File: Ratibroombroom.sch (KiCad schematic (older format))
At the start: 116 parts, among them J1 Conn_01x02_Male, J10 Conn_01x04_Male, J11 Conn_01x04_Male, J12 Support board base, J13 Support board base, J2 Conn_01x02_Male, J3 Conn_01x10_Male, J4 Support board axle, J5 Conn_01x02_Male, J6 Conn_01x02_Male, J7 Support board axle, J8 Conn_01x04_Male, J9 Conn_01x04_Male, Q1 IRLML6344, Q10 S8050, Q11 IRF7416PbF, Q2 IRLML6344, Q3 IRLML6344, Q4 IRLML6344, Q5 PT12-21B/TR8, Q6 PT12-21B/TR8, Q7 PT12-21B/TR8, Q8 PT12-21B/TR8, Q9 IRLML6344, SW1 B3U, SW2 B3U, SW3 PCM12, U1 AZ1117-3.3, U2 DRV8835, U3 AS5145B-HSST, U4 MPU-9250, U5 STM32F405RGTx, U6 AS5145B-HSST, U7 DRV8835, U8 L6932D1.2TR, U9 L6932D1.2TR, Y1 8MHZ

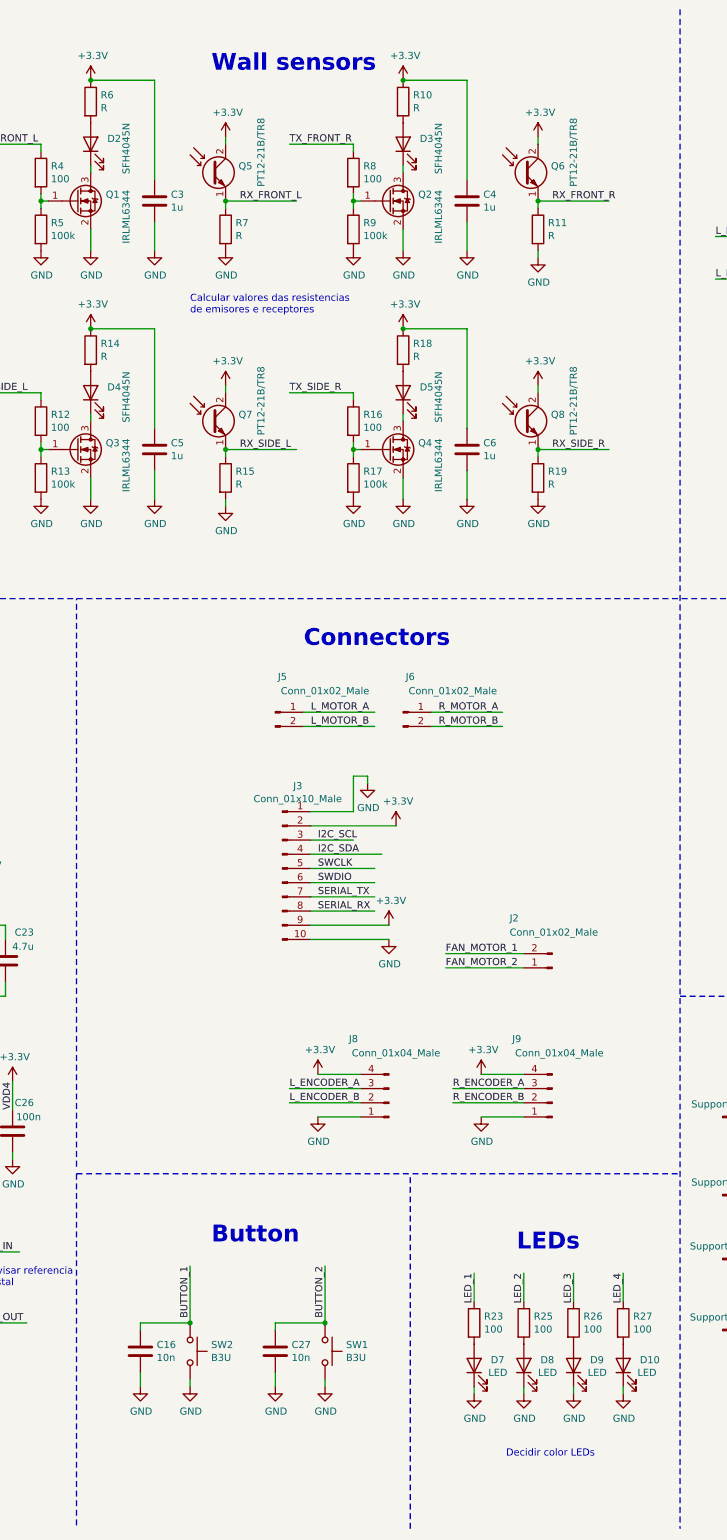
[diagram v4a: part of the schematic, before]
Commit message: Add BOM references
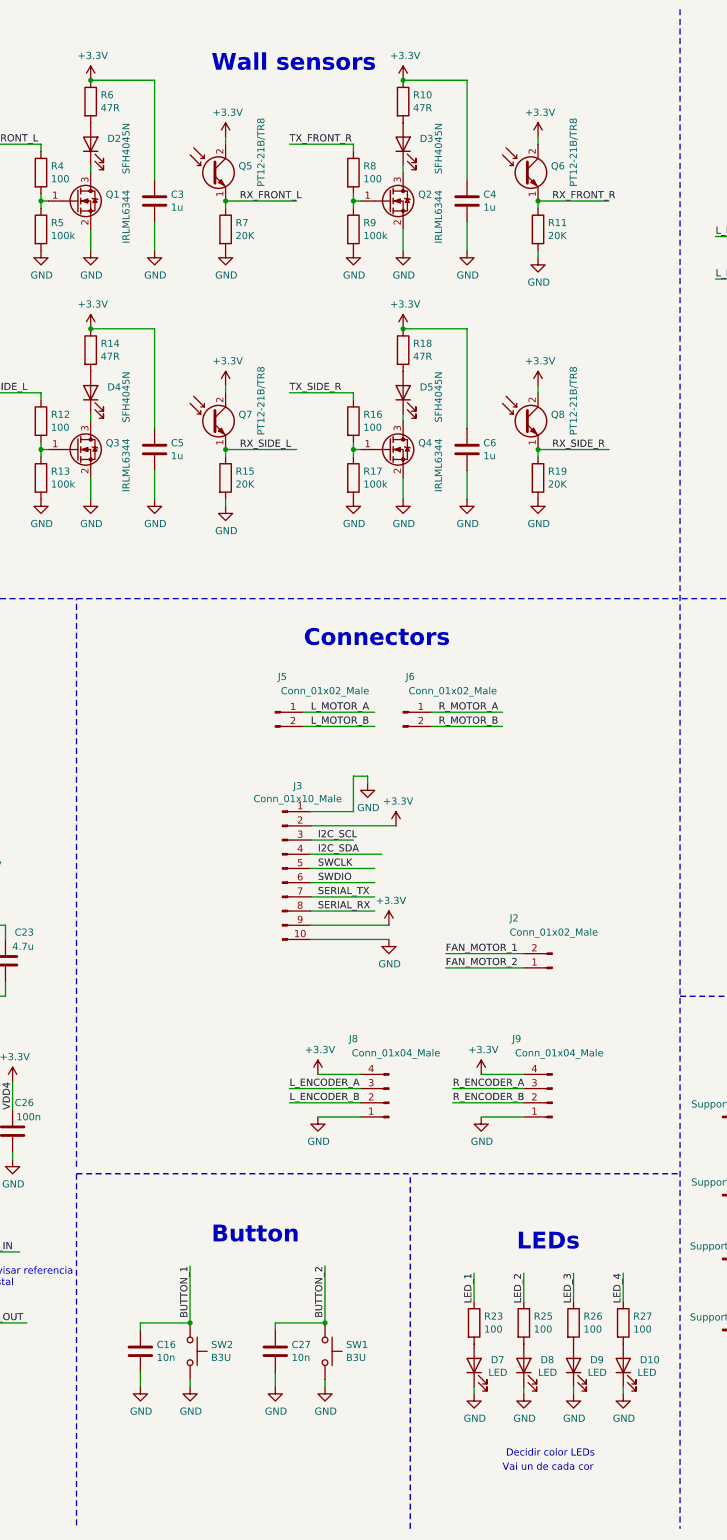
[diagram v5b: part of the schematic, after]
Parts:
- D10: MFR (none) -> 19-217/BHC-ZL1M2RY/3T; Note (none) -> Blue
- D7: MFR (none) -> LTW-C193DS5; Note (none) -> White
- D8: MFR (none) -> 19-217/R6C-AL1M2VY/3T; Note (none) -> Red
- D9: MFR (none) -> ORH-G36G; Note (none) -> Green
- J3: MFR (none) -> 20021111-00010T4LF; Note (none) -> Female: 2343U-205CNG1SNT01
- R10, R14, R18, R6: value R -> 47R; MFR (none) -> CR0603FA47R0G
- R11, R15, R19, R7: value R -> 20K; MFR (none) -> RK73H1JTTD2002F
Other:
- note added: "Vai un de cada cor"
- note removed: "Calcular valores das resistencias\nde emisores e receptores"
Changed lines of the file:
@@
 P 7150 2050
 F 0 "R7" H 7220 2096 50  0000 L CNN
-F 1 "R" H 7220 2005 50  0000 L CNN
+F 1 "20K" H 7220 2005 50  0000 L CNN
 F 2 "Resistor_SMD:R_0603_1608Metric" V 7080 2050 50  0001 C CNN
 F 3 "~" H 7150 2050 50  0001 C CNN
+F 4 "RK73H1JTTD2002F" H 7150 2050 50  0001 C CNN "MFR"
 	1    7150 2050
 	1    0    0    -1
@@
 P 6200 1150
 F 0 "R6" H 6270 1196 50  0000 L CNN
-F 1 "R" H 6270 1105 50  0000 L CNN
+F 1 "47R" H 6270 1105 50  0000 L CNN
 F 2 "Resistor_SMD:R_0603_1608Metric" V 6130 1150 50  0001 C CNN
 F 3 "~" H 6200 1150 50  0001 C CNN
+F 4 "CR0603FA47R0G" H 6200 1150 50  0001 C CNN "MFR"
 	1    6200 1150
 	1    0    0    -1
@@
 P 9350 2050
 F 0 "R11" H 9420 2096 50  0000 L CNN
-F 1 "R" H 9420 2005 50  0000 L CNN
+F 1 "20K" H 9420 2005 50  0000 L CNN
 F 2 "Resistor_SMD:R_0603_1608Metric" V 9280 2050 50  0001 C CNN
 F 3 "~" H 9350 2050 50  0001 C CNN
+F 4 "RK73H1JTTD2002F" H 9350 2050 50  0001 C CNN "MFR"
 	1    9350 2050
 	1    0    0    -1
@@
 P 8400 1150
 F 0 "R10" H 8470 1196 50  0000 L CNN
-F 1 "R" H 8470 1105 50  0000 L CNN
+F 1 "47R" H 8470 1105 50  0000 L CNN
 F 2 "Resistor_SMD:R_0603_1608Metric" V 8330 1150 50  0001 C CNN
 F 3 "~" H 8400 1150 50  0001 C CNN
+F 4 "CR0603FA47R0G" H 8400 1150 50  0001 C CNN "MFR"
 	1    8400 1150
 	1    0    0    -1
@@
 P 7150 3800
 F 0 "R15" H 7220 3846 50  0000 L CNN
-F 1 "R" H 7220 3755 50  0000 L CNN
+F 1 "20K" H 7220 3755 50  0000 L CNN
 F 2 "Resistor_SMD:R_0603_1608Metric" V 7080 3800 50  0001 C CNN
 F 3 "~" H 7150 3800 50  0001 C CNN
+F 4 "RK73H1JTTD2002F" H 7150 3800 50  0001 C CNN "MFR"
 	1    7150 3800
 	1    0    0    -1
@@
 P 6200 2900
 F 0 "R14" H 6270 2946 50  0000 L CNN
-F 1 "R" H 6270 2855 50  0000 L CNN
+F 1 "47R" H 6270 2855 50  0000 L CNN
 F 2 "Resistor_SMD:R_0603_1608Metric" V 6130 2900 50  0001 C CNN
 F 3 "~" H 6200 2900 50  0001 C CNN
+F 4 "CR0603FA47R0G" H 6200 2900 50  0001 C CNN "MFR"
 	1    6200 2900
 	1    0    0    -1
@@
 P 9350 3800
 F 0 "R19" H 9420 3846 50  0000 L CNN
-F 1 "R" H 9420 3755 50  0000 L CNN
+F 1 "20K" H 9420 3755 50  0000 L CNN
 F 2 "Resistor_SMD:R_0603_1608Metric" V 9280 3800 50  0001 C CNN
 F 3 "~" H 9350 3800 50  0001 C CNN
+F 4 "RK73H1JTTD2002F" H 9350 3800 50  0001 C CNN "MFR"
 	1    9350 3800
 	1    0    0    -1
@@
 P 8400 2900
 F 0 "R18" H 8470 2946 50  0000 L CNN
-F 1 "R" H 8470 2855 50  0000 L CNN
+F 1 "47R" H 8470 2855 50  0000 L CNN
 F 2 "Resistor_SMD:R_0603_1608Metric" V 8330 2900 50  0001 C CNN
 F 3 "~" H 8400 2900 50  0001 C CNN
+F 4 "CR0603FA47R0G" H 8400 2900 50  0001 C CNN "MFR"
 	1    8400 2900
 	1    0    0    -1
@@
 F 2 "LED_SMD:LED_0603_1608Metric" H 8900 10050 50  0001 C CNN
 F 3 "~" H 8900 10050 50  0001 C CNN
+F 4 "LTW-C193DS5" V 8900 10050 50  0001 C CNN "MFR"
+F 5 "White" V 8900 10050 50  0001 C CNN "Note"
 	1    8900 10050
 	0    -1   -1   0
@@
 F 2 "LED_SMD:LED_0603_1608Metric" H 9250 10050 50  0001 C CNN
 F 3 "~" H 9250 10050 50  0001 C CNN
+F 4 "19-217/R6C-AL1M2VY/3T" V 9250 10050 50  0001 C CNN "MFR"
+F 5 "Red" V 9250 10050 50  0001 C CNN "Note"
 	1    9250 10050
 	0    -1   -1   0
@@
 F 2 "LED_SMD:LED_0603_1608Metric" H 9600 10050 50  0001 C CNN
 F 3 "~" H 9600 10050 50  0001 C CNN
+F 4 "ORH-G36G" V 9600 10050 50  0001 C CNN "MFR"
+F 5 "Green" V 9600 10050 50  0001 C CNN "Note"
 	1    9600 10050
 	0    -1   -1   0
@@
 F 2 "LED_SMD:LED_0603_1608Metric" H 9950 10050 50  0001 C CNN
 F 3 "~" H 9950 10050 50  0001 C CNN
+F 4 "19-217/BHC-ZL1M2RY/3T" V 9950 10050 50  0001 C CNN "MFR"
+F 5 "Blue" V 9950 10050 50  0001 C CNN "Note"
 	1    9950 10050
 	0    -1   -1   0
@@
 	1    0    0    -1
 $EndComp
-Text Notes 6900 2650 0    50   ~ 0
-Calcular valores das resistencias\nde emisores e receptores
 $Comp
 L Connector:Conn_01x10_Male J3
@@
 F 2 "Connector_PinHeader_1.27mm:PinHeader_2x05_P1.27mm_Vertical" H 7550 6550 50  0001 C CNN
 F 3 "~" H 7550 6550 50  0001 C CNN
+F 4 "20021111-00010T4LF" H 7550 6550 50  0001 C CNN "MFR"
+F 5 "Female: 2343U-205CNG1SNT01" H 7550 6550 50  0001 C CNN "Note"
 	1    7550 6550
 	1    0    0    -1
@@
 Wire Wire Line
 	10950 9300 10850 9300
+Text Notes 9100 10800 0    50   ~ 0
+Vai un de cada cor
 $EndSCHEMATC

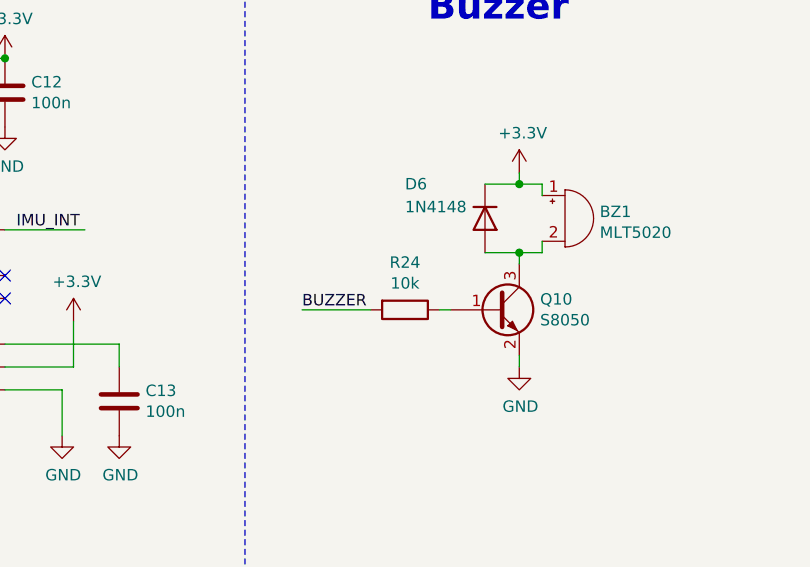
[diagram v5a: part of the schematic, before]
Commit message: Change R24 value to 1k8 to increase buzzer loudness
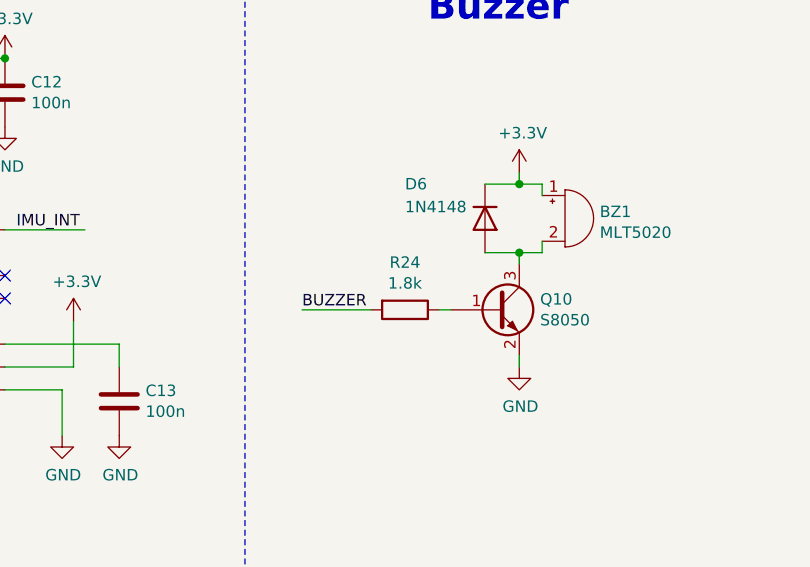
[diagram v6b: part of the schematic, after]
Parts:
- R24: value 10k -> 1.8k; MFR CR0603FA1002G -> 0603WAD1801T5E
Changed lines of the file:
@@
 P 14300 6250
 F 0 "R24" V 14093 6250 50  0000 C CNN
-F 1 "10k" V 14184 6250 50  0000 C CNN
+F 1 "1.8k" V 14184 6250 50  0000 C CNN
 F 2 "Resistor_SMD:R_0603_1608Metric" V 14230 6250 50  0001 C CNN
 F 3 "~" H 14300 6250 50  0001 C CNN
-F 4 "CR0603FA1002G" V 14300 6250 50  0001 C CNN "MFR"
+F 4 "0603WAD1801T5E" V 14300 6250 50  0001 C CNN "MFR"
 	1    14300 6250
 	0    1    1    0
